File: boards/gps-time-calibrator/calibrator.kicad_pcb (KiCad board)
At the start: 4 copper layers, 180 x 100 mm, 368 parts, among them J1 DF40C-40DP-0.4V(51), J2 DF40C(2.0)-40DS-0.4V(51), J3 USB-C 5V/3A + DATA, J5 GPS ANTENNA, J6 INPUT 5V / 2.5V THRESHOLD, J7 FPGA OUTPUT 5V, J8 61300411121, Q1 AO3400A, Q10 AO3400A, Q11 AO3400A, Q12 AO3400A, Q13 AO3400A, Q14 AO3400A, Q15 AO3400A, Q16 AO3400A, Q2 AO3400A, Q3 AO3400A, Q4 AO3400A, Q5 AO3400A, Q6 AO3400A, Q7 AO3400A, Q8 AO3400A, Q9 AO3400A, U1 USBLC6-2SC6, U10 SN74AHCT1G125DBVR, U11 HUSB238_002DD, U14 TPS259531DSGR, U15 TPS7A4533DCQR, U2 AP2112K-3.3, U3 SN74LVC541APWR, U4 SN74LVC541APWR, U5 AP2112K-3.3, U6 MAX-M10S-00B-01, U7 SN74LVC1G17DBVR, U9 TLV3501AIDBVR, Y1 AOC97FAJC-10.0000

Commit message: Escape CC1/CC2 under the USB-C receptacle on F.Cu
Both CC lines leave J3 eastward beneath the receptacle body, run north
between the shell legs and come round to U11 on the top layer, replacing
the four vias and In1 runs. The nested lanes land swapped at U11 (J3 A5 ->
pin 5, B5 -> pin 4) so they never cross; the HUSB238 resolves orientation
from either CC pin. The A12 shell-ground stub now lands in S1, and S1 gets a
short tie to a stitching via since the lanes cut off its old pour path.

Co-Authored-By: Claude Opus 5.5 <noreply@anthropic.com>
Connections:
- U11 pad 4: CC1 -> CC2
- U11 pad 5: CC2 -> CC1
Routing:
- net CC1: track 14.1 -> 19.3 mm, vias 2 -> 0
- net GND: track 178.5 -> 181.9 mm, vias 148 -> 149
- net CC2: track 11.5 -> 14.6 mm, vias 2 -> 0
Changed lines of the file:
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@@
 			(layers "F.Cu" "F.Mask" "F.Paste")
 			(roundrect_rratio 0.25)
-			(net "CC1")
+			(net "CC2")
 		)
 		(pad "5" smd roundrect
@@
 			(layers "F.Cu" "F.Mask" "F.Paste")
 			(roundrect_rratio 0.25)
-			(net "CC2")
+			(net "CC1")
 		)
 		(pad "6" smd roundrect
@@
 	)
 	(segment
+		(start 194.07 25.68)
+		(end 194.07 23.6)
+		(width 0.4)
+		(layer "F.Cu")
+		(net "GND")
+	)
+	(segment
 		(start 79.05 37.062)
 		(end 77.75 37.062)
@@
 	(segment
 		(start 193.155 26.75)
-		(end 193.6 26.75)
+		(end 193.9 26.75)
+		(width 0.3)
+		(layer "F.Cu")
+		(net "GND")
+	)
+	(segment
+		(start 193.9 26.75)
+		(end 193.9 25.68)
 		(width 0.3)
 		(layer "F.Cu")
@@
 	)
 	(via
+		(at 194.07 23.6)
+		(size 0.5)
+		(drill 0.25)
+		(layers "F.Cu" "B.Cu")
+		(net "GND")
+	)
+	(via
 		(at 118.5 49.6)
 		(size 0.5)
@@
 	)
 	(segment
-		(start 193.155 31.25)
-		(end 191.2 31.25)
+		(start 196.4 23.7)
+		(end 192.7 20)
 		(width 0.2)
 		(layer "F.Cu")
@@
 	)
 	(segment
-		(start 190.6 20.5)
-		(end 189.475 20.5)
+		(start 193.155 31.25)
+		(end 196.4 31.25)
 		(width 0.2)
 		(layer "F.Cu")
 		(net "CC1")
 	)
-	(via
-		(at 190.6 20.5)
-		(size 0.5)
-		(drill 0.25)
-		(layers "F.Cu" "B.Cu")
-		(net "CC1")
-	)
-	(via
-		(at 191.2 31.25)
-		(size 0.5)
-		(drill 0.25)
-		(layers "F.Cu" "B.Cu")
-		(net "CC1")
-	)
 	(segment
-		(start 190.6 30.65)
-		(end 190.6 20.5)
+		(start 192.7 20)
+		(end 189.475 20)
 		(width 0.2)
-		(layer "In1.Cu")
+		(layer "F.Cu")
 		(net "CC1")
 	)
 	(segment
-		(start 191.2 31.25)
-		(end 190.6 30.65)
+		(start 196.4 31.25)
+		(end 196.4 23.7)
 		(width 0.2)
-		(layer "In1.Cu")
+		(layer "F.Cu")
 		(net "CC1")
 	)
 	(segment
-		(start 191.25 20)
-		(end 189.475 20)
+		(start 195.7 28.25)
+		(end 195.7 23.8)
 		(width 0.2)
 		(layer "F.Cu")
@@
 	)
 	(segment
-		(start 193.155 28.25)
-		(end 191.95 28.25)
+		(start 192.4 20.5)
+		(end 189.475 20.5)
 		(width 0.2)
 		(layer "F.Cu")
 		(net "CC2")
 	)
-	(via
-		(at 191.95 28.25)
-		(size 0.5)
-		(drill 0.25)
-		(layers "F.Cu" "B.Cu")
-		(net "CC2")
-	)
-	(via
-		(at 191.25 20)
-		(size 0.5)
-		(drill 0.25)
-		(layers "F.Cu" "B.Cu")
-		(net "CC2")
-	)
 	(segment
-		(start 191.95 28.25)
-		(end 191.25 27.55)
+		(start 193.155 28.25)
+		(end 195.7 28.25)
 		(width 0.2)
-		(layer "In1.Cu")
+		(layer "F.Cu")
 		(net "CC2")
 	)
 	(segment
-		(start 191.25 27.55)
-		(end 191.25 20)
+		(start 195.7 23.8)
+		(end 192.4 20.5)
 		(width 0.2)
-		(layer "In1.Cu")
+		(layer "F.Cu")
 		(net "CC2")
 	)

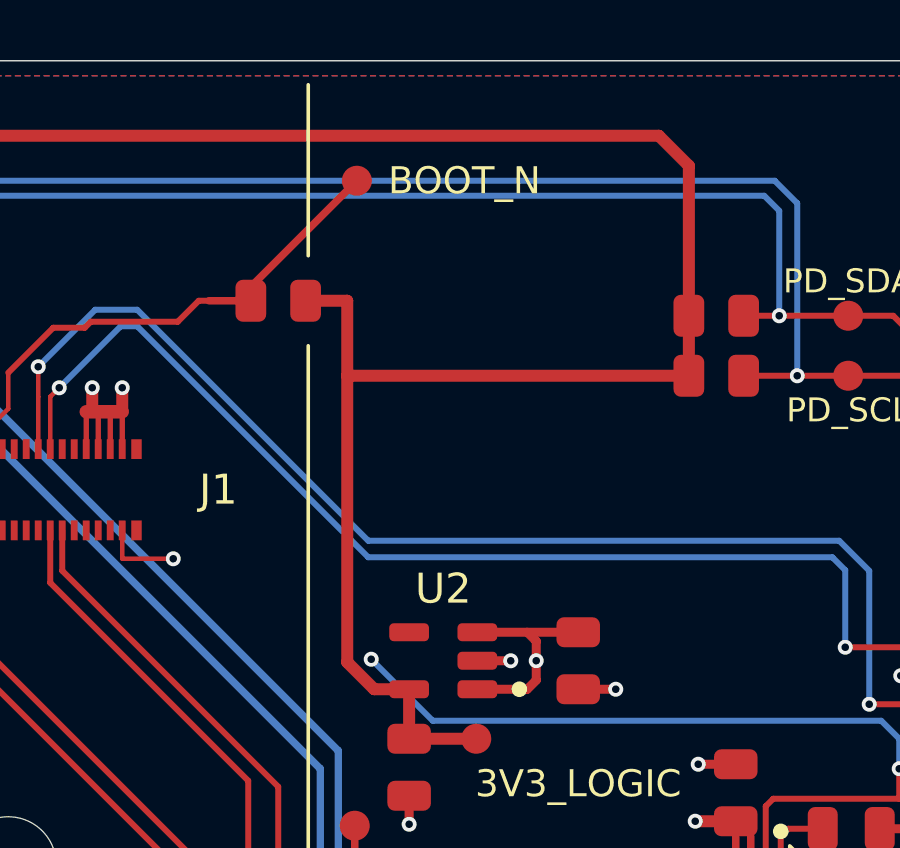
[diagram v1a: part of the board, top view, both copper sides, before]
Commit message: Move the BOOT pull-up R4 onto the +3V3 rail beside the PD pull-ups
R4 now sits on the x 177.69 +3V3_LOGIC rail next to R167/R168, so the
rail spur that fed it at (164,18) is gone and the rail corner gets a 45°
chamfer. BOOT runs J1 -> TP65 -> R4 on F.Cu, making TP65 an inline test
point and removing the overlapping/acute BOOT stubs at the old pad.

Co-Authored-By: Claude Opus 5.5 <noreply@anthropic.com>
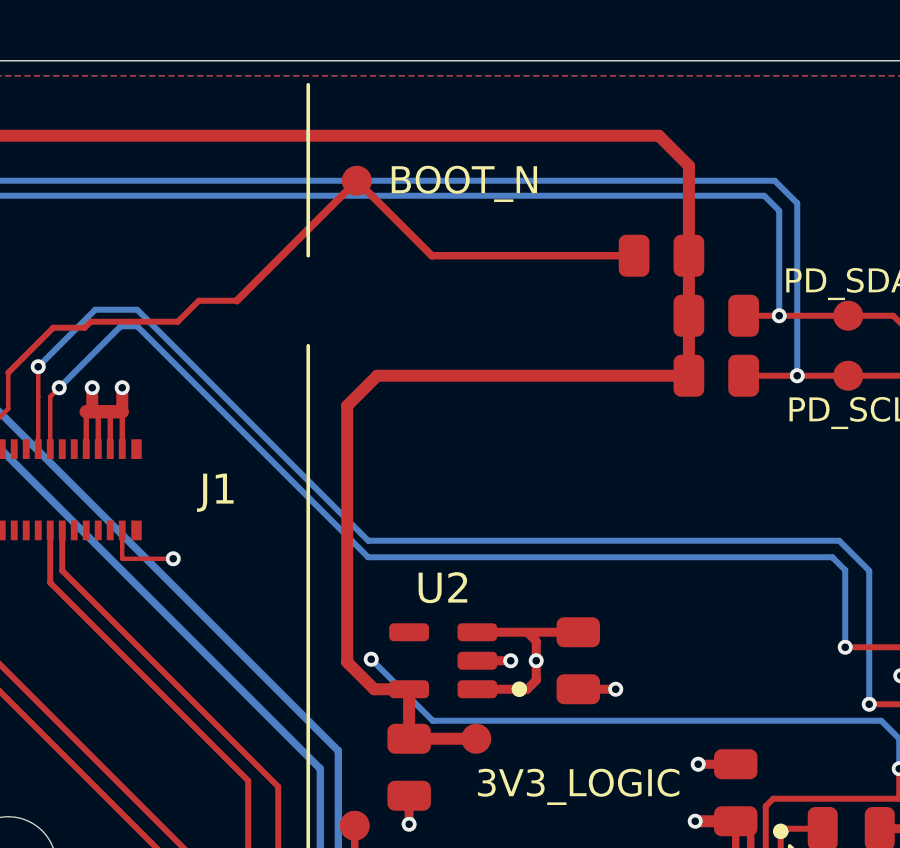
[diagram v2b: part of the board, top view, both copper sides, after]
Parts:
- moved R4 12.9 mm to (176.8, 16.5)
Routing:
- net ESP_GPIO0_BOOT: track 17.6 -> 27.3 mm
- net +3V3_LOGIC: track 258.5 -> 254.0 mm
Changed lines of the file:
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@@
 	(footprint "Calibrator:R_0805_2012Metric"
 		(layer "F.Cu")
-		(at 164 18)
+		(at 176.7755 16.5)
 		(descr "100 kOhm pull-up holding ESP32 GPIO0 (boot strap) high for normal run.")
 		(tags "resistor")
 		(property "Reference" "R4"
-			(at 0 -1.65 0)
+			(at 0 -0.65 0)
 			(layer "F.SilkS")
 			(hide yes)
@@
 	)
 	(segment
-		(start 177.6875 20.5)
-		(end 166.3 20.5)
+		(start 166.3 30.05)
+		(end 166.3 21.5)
 		(width 0.4)
 		(layer "F.Cu")
@@
 	)
 	(segment
+		(start 166.3 21.5)
+		(end 167.3 20.5)
+		(width 0.4)
+		(layer "F.Cu")
+		(net "+3V3_LOGIC")
+	)
+	(segment
 		(start 114.088 23.8)
 		(end 115.651 25.363)
@@
 	)
 	(segment
+		(start 167.3 20.5)
+		(end 177.6875 20.5)
+		(width 0.4)
+		(layer "F.Cu")
+		(net "+3V3_LOGIC")
+	)
+	(segment
 		(start 176.6875 12.5)
 		(end 137.4 12.5)
@@
 	)
 	(segment
-		(start 166.3 30.05)
-		(end 166.3 18)
-		(width 0.4)
-		(layer "F.Cu")
-		(net "+3V3_LOGIC")
-	)
-	(segment
 		(start 167.2 30.95)
 		(end 166.3 30.05)
@@
 		(net "+3V3_LOGIC")
 	)
-	(segment
-		(start 164.9125 18)
-		(end 166.3 18)
-		(width 0.4)
-		(layer "F.Cu")
-		(net "+3V3_LOGIC")
-	)
 	(via
 		(at 130.4 30)
@@
 	)
 	(segment
-		(start 161.35 18)
-		(end 161.7 18)
-		(width 0.2)
+		(start 166.621 14)
+		(end 169.121 16.5)
+		(width 0.25)
 		(layer "F.Cu")
 		(net "ESP_GPIO0_BOOT")
@@
 	)
 	(segment
-		(start 163.0875 18)
-		(end 161.6875 18)
+		(start 169.121 16.5)
+		(end 175.863 16.5)
 		(width 0.25)
 		(layer "F.Cu")
@@
 	)
 	(segment
-		(start 161.7 18)
-		(end 161.6875 18)
-		(width 0.2)
-		(layer "F.Cu")
-		(net "ESP_GPIO0_BOOT")
-	)
-	(segment
 		(start 157.75 18.7)
 		(end 160.65 18.7)
@@
 		(width 0.2)
 		(layer "F.Cu")
+		(net "ESP_GPIO0_BOOT")
+	)
+	(segment
+		(start 161.35 18)
+		(end 162.621 18)
+		(width 0.2)
+		(layer "F.Cu")

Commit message: Place the BOOT pull-up R4 at J1 and drop the GPIO0 test pad TP65
R4 now stands vertically just north of J1 pin 12: BOOT exits the
connector straight into R4 pad 1 and pad 2 tees into the +3V3_LOGIC
F.Cu strip at y 12.5. The 10 mm BOOT run across the module footprint
and the TP65 probe pad are gone; GPIO0 recovery uses R4 pad 1.

TP65 is removed from circuit.json, the schematic/PDF, part descriptions
and the test-point docs and audit (27 -> 26 pads).

Co-Authored-By: Claude Opus 5.5 <noreply@anthropic.com>
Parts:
- removed TP65: BOOT_N, Calibrator:TP_1p0mm
- moved R4 20.3 mm to (156.5, 17.0), turned to 90 degrees
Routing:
- net ESP_GPIO0_BOOT: track 27.3 -> 5.90 mm
- net +3V3_LOGIC: track 254.0 -> 257.6 mm
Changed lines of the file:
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@@
 		)
 	)
-	(footprint "Calibrator:TP_1p0mm"
-		(layer "F.Cu")
-		(at 166.6208 14)
-		(descr "Test pad: ESP32 GPIO0 boot strap.")
-		(property "Reference" "TP65"
-			(at 0 -2 0)
-			(layer "F.SilkS")
-			(hide yes)
-			(effects
-				(font
-					(size 0.9 0.9)
-					(thickness 0.15)
-				)
-			)
-		)
-		(property "Value" "BOOT_N"
-			(at 3.585 0 0)
-			(layer "F.SilkS")
-			(effects
-				(font
-					(size 0.9 0.9)
-					(thickness 0.15)
-				)
-			)
-		)
-		(property "Datasheet" ""
-			(at 0 0 0)
-			(layer "F.Fab")
-			(hide yes)
-			(effects
-				(font
-					(size 1.27 1.27)
-				)
-			)
-		)
-		(property "Description" ""
-			(at 0 0 0)
-			(layer "F.Fab")
-			(hide yes)
-			(effects
-				(font
-					(size 1.27 1.27)
-				)
-			)
-		)
-		(attr smd exclude_from_pos_files exclude_from_bom)
-		(duplicate_pad_numbers_are_jumpers no)
-		(pad "1" smd circle
-			(at 0 0)
-			(size 1 1)
-			(layers "F.Cu" "F.Mask")
-			(net "ESP_GPIO0_BOOT")
-			(solder_mask_margin 0.05)
-			(zone_connect 2)
-		)
-		(embedded_fonts no)
-	)
 	(footprint "Calibrator:R_0805_2012Metric"
 		(layer "F.Cu")
@@
 	(footprint "Calibrator:R_0805_2012Metric"
 		(layer "F.Cu")
-		(at 176.7755 16.5)
+		(at 156.5 17 90)
 		(descr "100 kOhm pull-up holding ESP32 GPIO0 (boot strap) high for normal run.")
 		(tags "resistor")
 		(property "Reference" "R4"
-			(at 0 -0.65 0)
+			(at 0 -1.3 90)
 			(layer "F.SilkS")
 			(hide yes)
@@
 		)
 		(property "Value" "100k"
-			(at 0 1.65 0)
+			(at 0 1.65 90)
 			(layer "F.Fab")
 			(hide yes)
@@
 		)
 		(property "Datasheet" ""
-			(at 0 0 0)
+			(at 0 0 90)
 			(layer "F.Fab")
 			(hide yes)
@@
 		)
 		(property "Description" ""
-			(at 0 0 0)
+			(at 0 0 90)
 			(layer "F.Fab")
 			(hide yes)
@@
 		)
 		(property "MPN" "RC0805FR-07100KL"
-			(at 0 0 0)
+			(at 0 0 90)
 			(layer "F.SilkS")
 			(hide yes)
@@
 		)
 		(property "LCSC" "C96346"
-			(at 0 0 0)
+			(at 0 0 90)
 			(layer "F.SilkS")
 			(hide yes)
@@
 		)
 		(property "Assembly" "JLCPCB"
-			(at 0 0 0)
+			(at 0 0 90)
 			(layer "F.SilkS")
 			(hide yes)
@@
 		)
 		(property "Supplier URL" ""
-			(at 0 0 0)
+			(at 0 0 90)
 			(layer "F.SilkS")
 			(hide yes)
@@
 		(duplicate_pad_numbers_are_jumpers no)
 		(fp_line
-			(start -1.68 -0.95)
-			(end 1.68 -0.95)
+			(start 1.68 -0.95)
+			(end 1.68 0.95)
 			(stroke
 				(width 0.05)
@@
 		)
 		(fp_line
-			(start -1.68 0.95)
-			(end -1.68 -0.95)
+			(start -1.68 -0.95)
+			(end 1.68 -0.95)
 			(stroke
 				(width 0.05)
@@
 		)
 		(fp_line
-			(start 1.68 -0.95)
-			(end 1.68 0.95)
+			(start 1.68 0.95)
+			(end -1.68 0.95)
 			(stroke
 				(width 0.05)
@@
 		)
 		(fp_line
-			(start 1.68 0.95)
-			(end -1.68 0.95)
+			(start -1.68 0.95)
+			(end -1.68 -0.95)
 			(stroke
 				(width 0.05)
@@
 		)
 		(fp_line
-			(start -1 -0.625)
-			(end 1 -0.625)
+			(start 1 -0.625)
+			(end 1 0.625)
 			(stroke
 				(width 0.1)
@@
 		)
 		(fp_line
-			(start -1 0.625)
-			(end -1 -0.625)
+			(start -1 -0.625)
+			(end 1 -0.625)
 			(stroke
 				(width 0.1)
@@
 		)
 		(fp_line
-			(start 1 -0.625)
-			(end 1 0.625)
+			(start 1 0.625)
+			(end -1 0.625)
 			(stroke
 				(width 0.1)
@@
 		)
 		(fp_line
-			(start 1 0.625)
-			(end -1 0.625)
+			(start -1 0.625)
+			(end -1 -0.625)
 			(stroke
 				(width 0.1)
@@
 		)
 		(fp_text user "${REFERENCE}"
-			(at 0 0 0)
+			(at 0 0 90)
 			(layer "F.Fab")
 			(effects
@@
 		)
 		(pad "1" smd roundrect
-			(at -0.9125 0)
+			(at -0.9125 0 90)
 			(size 1.025 1.4)
 			(layers "F.Cu" "F.Mask" "F.Paste")
@@
 		)
 		(pad "2" smd roundrect
-			(at 0.9125 0)
+			(at 0.9125 0 90)
 			(size 1.025 1.4)
 			(layers "F.Cu" "F.Mask" "F.Paste")
@@
 	)
 	(segment
+		(start 156.5 16.087499)
+		(end 156.5 12.5)
+		(width 0.4)
+		(layer "F.Cu")
+		(net "+3V3_LOGIC")
+	)
+	(segment
 		(start 134.05 71)
 		(end 134.05 73.5)
@@
 	)
 	(segment
-		(start 166.621 14)
-		(end 169.121 16.5)
-		(width 0.25)
-		(layer "F.Cu")
-		(net "ESP_GPIO0_BOOT")
-	)
-	(segment
 		(start 155 21.6)
 		(end 155 20.4)
@@
 	)
 	(segment
-		(start 162.620833 18)
-		(end 166.6208 14)
-		(width 0.25)
-		(layer "F.Cu")
-		(net "ESP_GPIO0_BOOT")
-	)
-	(segment
-		(start 169.121 16.5)
-		(end 175.863 16.5)
-		(width 0.25)
-		(layer "F.Cu")
-		(net "ESP_GPIO0_BOOT")
-	)
-	(segment
-		(start 157.75 18.7)
-		(end 160.65 18.7)
-		(width 0.2)
-		(layer "F.Cu")
-		(net "ESP_GPIO0_BOOT")
-	)
-	(segment
-		(start 160.65 18.7)
-		(end 161.35 18)
+		(start 156.5 18.9)
+		(end 156.5 17.9125)
 		(width 0.2)
 		(layer "F.Cu")
@@
 	)
 	(segment
-		(start 156.5 18.9)
-		(end 157.55 18.9)
-		(width 0.2)
-		(layer "F.Cu")
-		(net "ESP_GPIO0_BOOT")
-	)
-	(segment
-		(start 161.35 18)
-		(end 162.621 18)
-		(width 0.2)
-		(layer "F.Cu")
-		(net "ESP_GPIO0_BOOT")
-	)
-	(segment
 		(start 154.400001 22.945)
 		(end 154.4 22.2)
@@
 		(layer "F.Cu")
 		(net "ESP_GPIO0_BOOT")
-	)
-	(segment
-		(start 157.55 18.9)
-		(end 157.75 18.7)
-		(width 0.2)
-		(layer "F.Cu")
-		(net "ESP_GPIO0_BOOT")
